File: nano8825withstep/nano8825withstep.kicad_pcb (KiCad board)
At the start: 2 copper layers, 14 parts, among them J1 Conn_01x02, J2 Conn_01x04, J3 Conn_01x04, J4 Conn_01x04, SW1 SW_DIP_x03, SW2 SW_DIP_x03, SW3 SW_DIP_x03

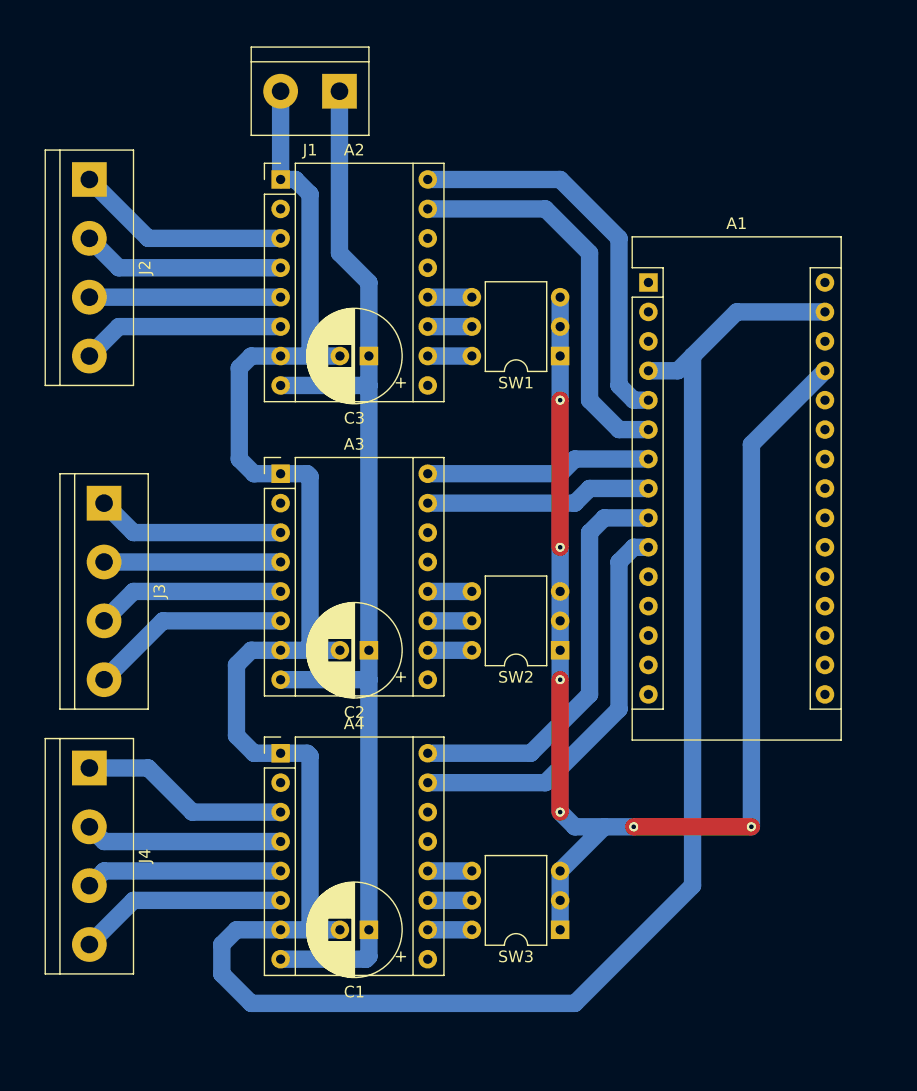
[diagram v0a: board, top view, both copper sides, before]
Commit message: Added limit and probe connectors
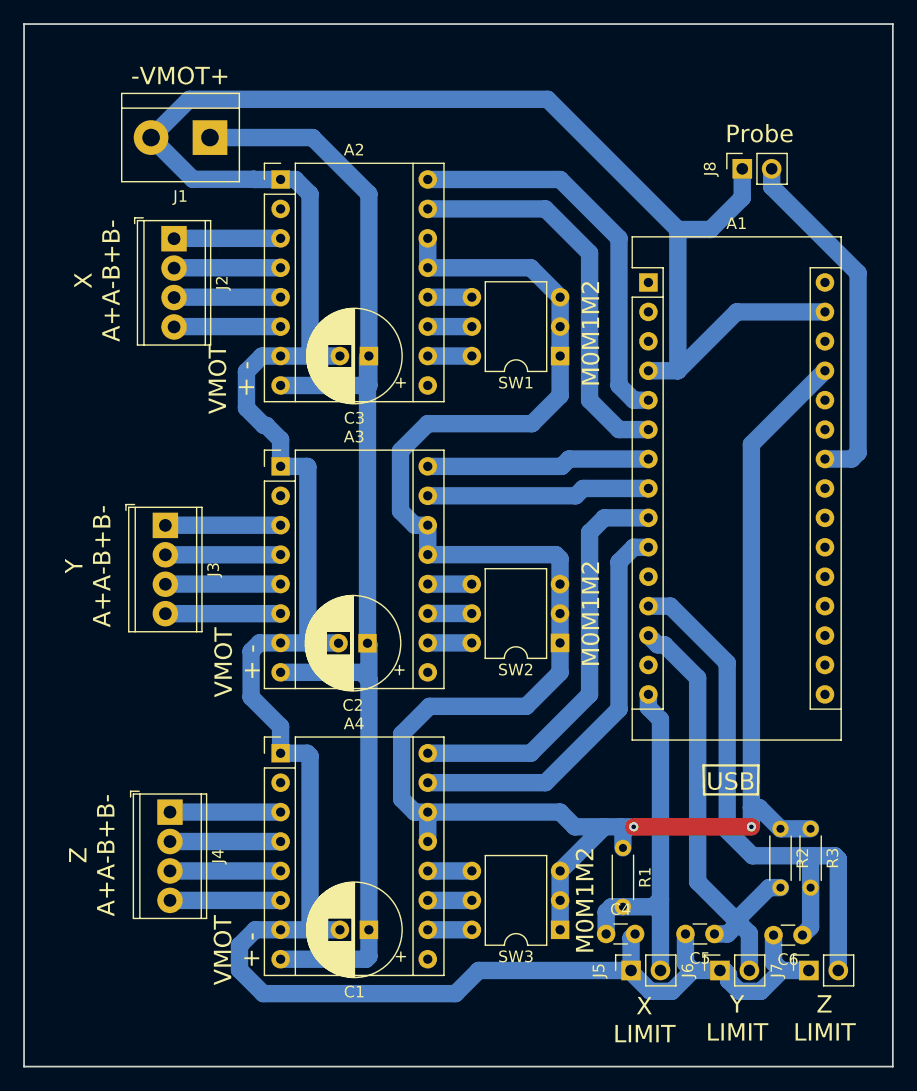
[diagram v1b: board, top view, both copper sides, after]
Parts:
- added C4: 100n, Capacitor_THT:C_Disc_D3.0mm_W1.6mm_P2.50mm, F.Cu at (85.2, 123.5)
- added C5: 100n, Capacitor_THT:C_Disc_D3.0mm_W1.6mm_P2.50mm, F.Cu at (94.6, 123.5)
- added C6: 100n, Capacitor_THT:C_Disc_D3.0mm_W1.6mm_P2.50mm, F.Cu at (102.2, 123.7)
- added J5: Conn_01x02, Connector_PinSocket_2.54mm:PinSocket_1x02_P2.54mm_Vertical, F.Cu at (87.4, 126.7)
- added J6: Conn_01x02, Connector_PinSocket_2.54mm:PinSocket_1x02_P2.54mm_Vertical, F.Cu at (95.1, 126.7)
- added J7: Conn_01x02, Connector_PinSocket_2.54mm:PinSocket_1x02_P2.54mm_Vertical, F.Cu at (102.8, 126.7)
- added J8: Conn_01x02_Female, Connector_PinSocket_2.54mm:PinSocket_1x02_P2.54mm_Vertical, F.Cu at (97.0, 57.5)
- added R1: 4k7, Resistor_THT:R_Axial_DIN0204_L3.6mm_D1.6mm_P5.08mm_Horizontal, F.Cu at (86.7, 116.1)
- added R2: 4k7, Resistor_THT:R_Axial_DIN0204_L3.6mm_D1.6mm_P5.08mm_Horizontal, F.Cu at (100.3, 114.5)
- added R3: 4k7, Resistor_THT:R_Axial_DIN0204_L3.6mm_D1.6mm_P5.08mm_Horizontal, F.Cu at (102.9, 114.5)
- J2, J3, J4: footprint TerminalBlock:TerminalBlock_bornier-4_P5.08mm -> TerminalBlock_Phoenix:TerminalBlock_Phoenix_MPT-0,5-4-2.54_1x04_P2.54mm_Horizontal
- moved J1 11.9 mm to (51.0, 54.8)
- moved J2 8.92 mm to (48.0, 63.5)
- moved J4 7.93 mm to (47.6, 113.0)
- moved J3 5.63 mm to (47.2, 88.3)
- moved A3 0.63 mm to (57.1, 83.2)
- moved SW2 0.63 mm to (81.3, 98.4)
- moved C2 0.62 mm to (64.7, 98.5)
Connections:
- A2 pad 13: Net-(A2-Pad13) -> Net-(A1-Pad27)
- A2 pad 14: Net-(A2-Pad14) -> Net-(A1-Pad27)
- A3 pad 13: Net-(A3-Pad13) -> Net-(A1-Pad27)
- A3 pad 14: Net-(A3-Pad14) -> Net-(A1-Pad27)
- A4 pad 13: Net-(A4-Pad13) -> Net-(A1-Pad27)
- A4 pad 14: Net-(A4-Pad14) -> Net-(A1-Pad27)
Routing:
- net Net-(A1-Pad27): track 114.0 -> 186.7 mm, vias 6 -> 2
- net Net-(A1-Pad12): track 0.00 -> 50.7 mm
- net Net-(A1-Pad29): track 223.2 -> 266.6 mm
- net Net-(A1-Pad13): track 0.00 -> 40.5 mm
- net Net-(A1-Pad15): track 0.00 -> 31.3 mm
- net Net-(A1-Pad24): track 0.00 -> 30.7 mm
- net Net-(A2-Pad3): track 18.6 -> 9.21 mm
- net Net-(A2-Pad8): track 98.7 -> 107.4 mm
- net Net-(A4-Pad3): track 18.1 -> 9.55 mm
- net Net-(A4-Pad6): track 18.1 -> 9.55 mm
- net Net-(A2-Pad4): track 17.6 -> 9.21 mm
- net Net-(A2-Pad6): track 17.6 -> 9.21 mm
- net Net-(A4-Pad5): track 17.0 -> 9.55 mm
- net Net-(A4-Pad4): track 17.0 -> 9.55 mm
- net Net-(A3-Pad6): track 17.3 -> 9.96 mm
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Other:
- board outline added: 75 x 90 mm
- board text added: "-VMOT+"
- board text added: "M0M1M2"
- board text added: "Probe"
- board text added: "USB"
- board text added: "VMOT + -"
- board text added: "X A+A-B+B-"
- board text added: "X LIMIT"
- board text added: "Y A+A-B+B-"
- board text added: "Y LIMIT"
- board text added: "Z A+A-B+B-"
- board text added: "Z LIMIT"
